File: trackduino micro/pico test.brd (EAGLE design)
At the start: 43.3 x 21.9 mm, 29 parts, among them IC2 74AHC1G125DBV, SW1 SPST_TACT-KMR2, U1 ATMEGA168MLF, X2 SMA-SMD, Y1 16MHZ

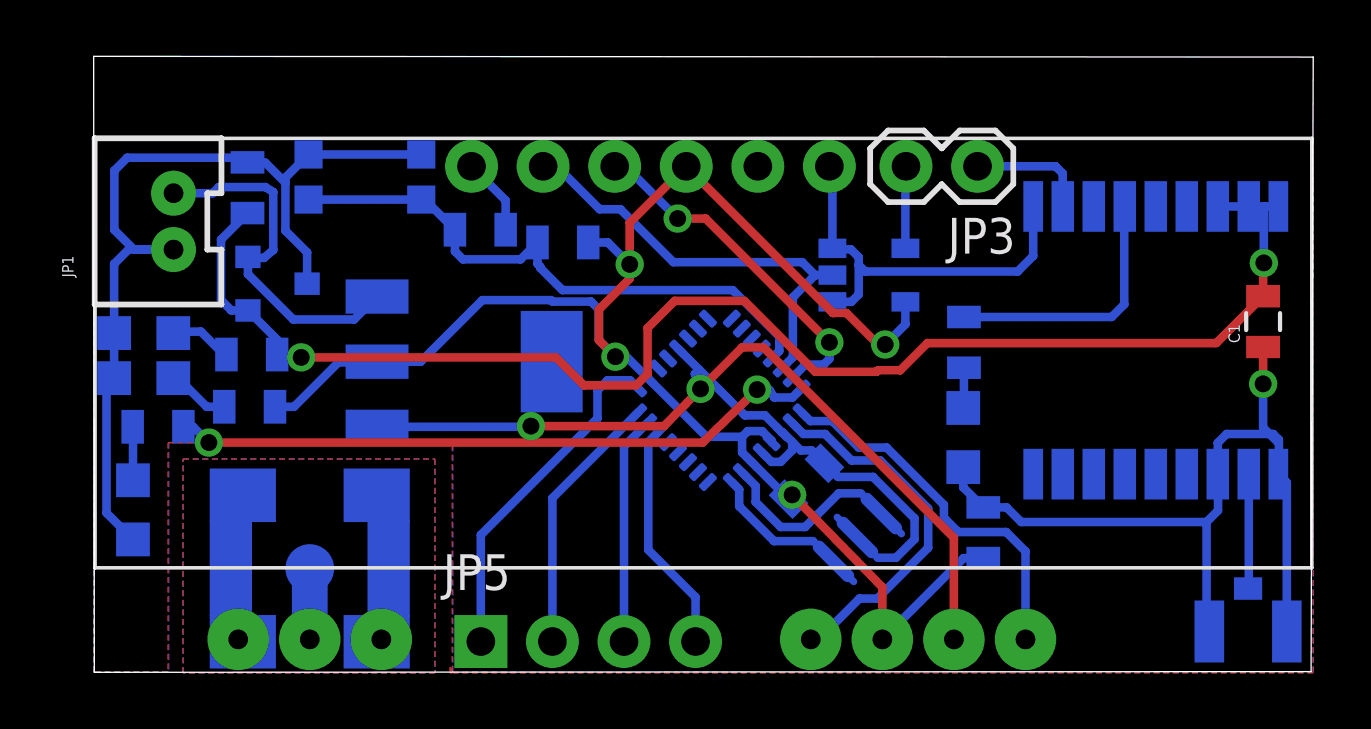
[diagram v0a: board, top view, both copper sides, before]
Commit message: minor fixes to smallest boards
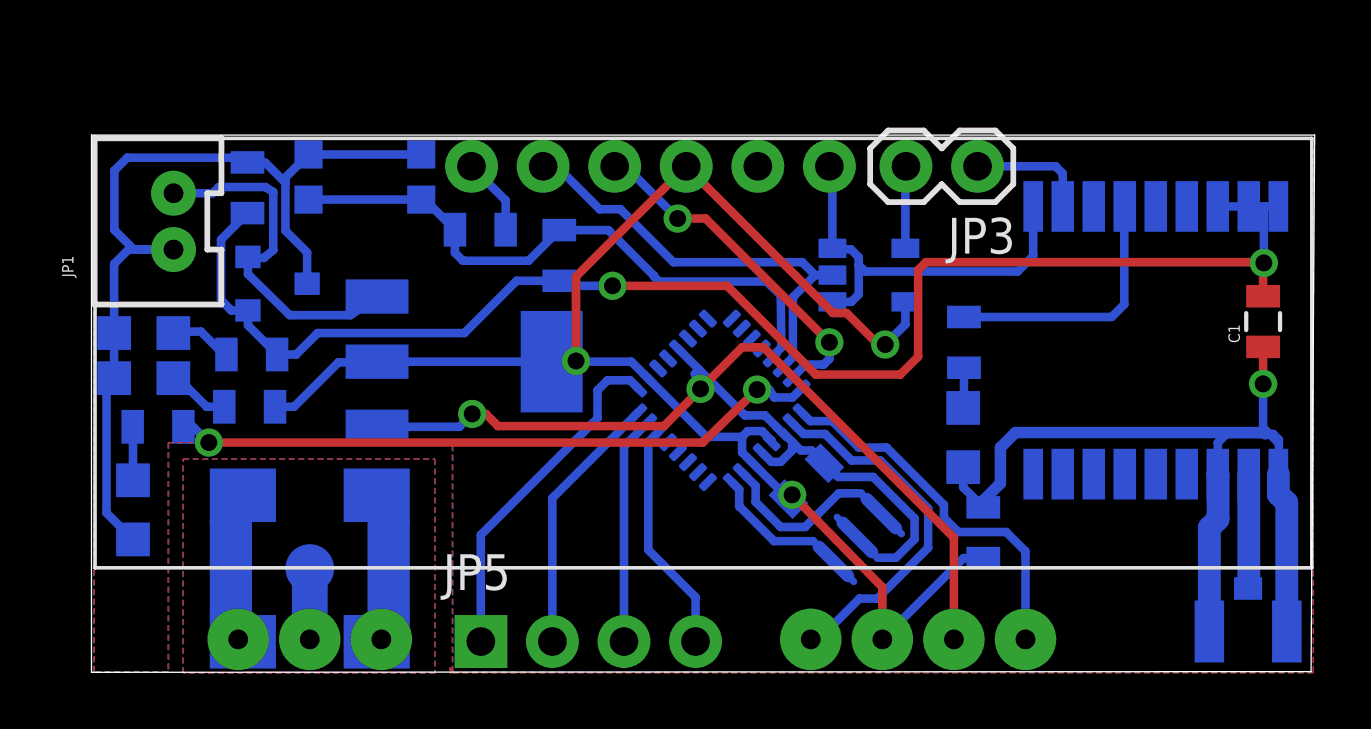
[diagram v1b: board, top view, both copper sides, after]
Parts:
- moved R5 0.48 mm to (68.0, 72.3), turned to 270 degrees
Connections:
- new net SCL: U1.28
- new net SDA: U1.27
- net 3V: now also R5.2
- net VCC: no longer R5.2
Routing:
- net GND: track 121.1 -> 141.6 mm
- net VCC: track 58.0 -> 54.0 mm, vias 4 -> 3
- net 3V: track 51.8 -> 52.9 mm
- net N$9: track 21.0 -> 21.9 mm
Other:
- board size 43.3 x 21.9 mm -> 43.4 x 19.1 mm
